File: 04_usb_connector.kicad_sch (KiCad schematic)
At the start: 2 parts

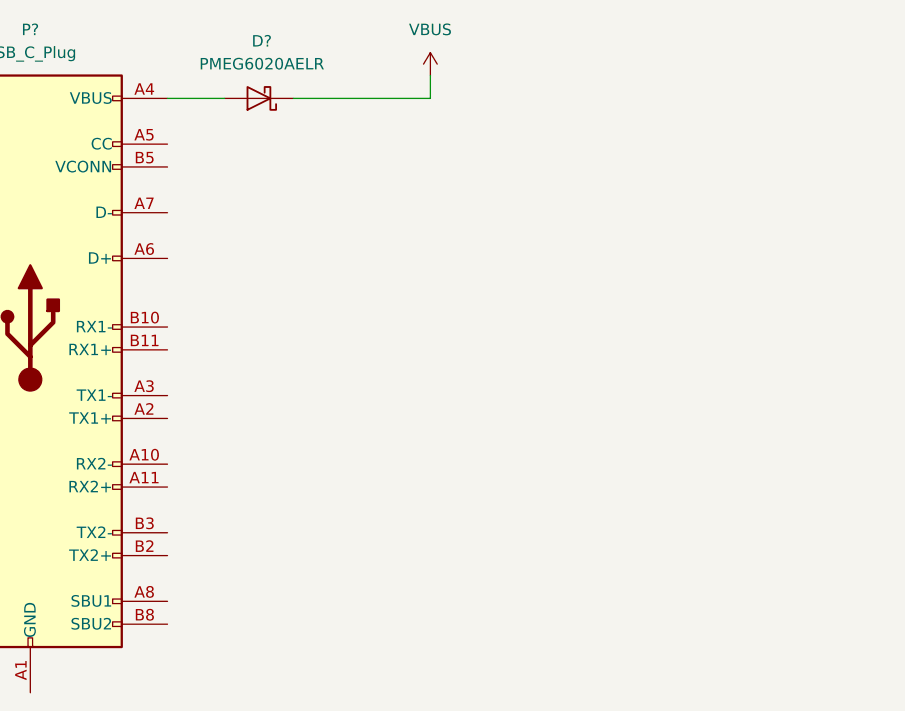
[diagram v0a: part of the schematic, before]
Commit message: added usb-c connector
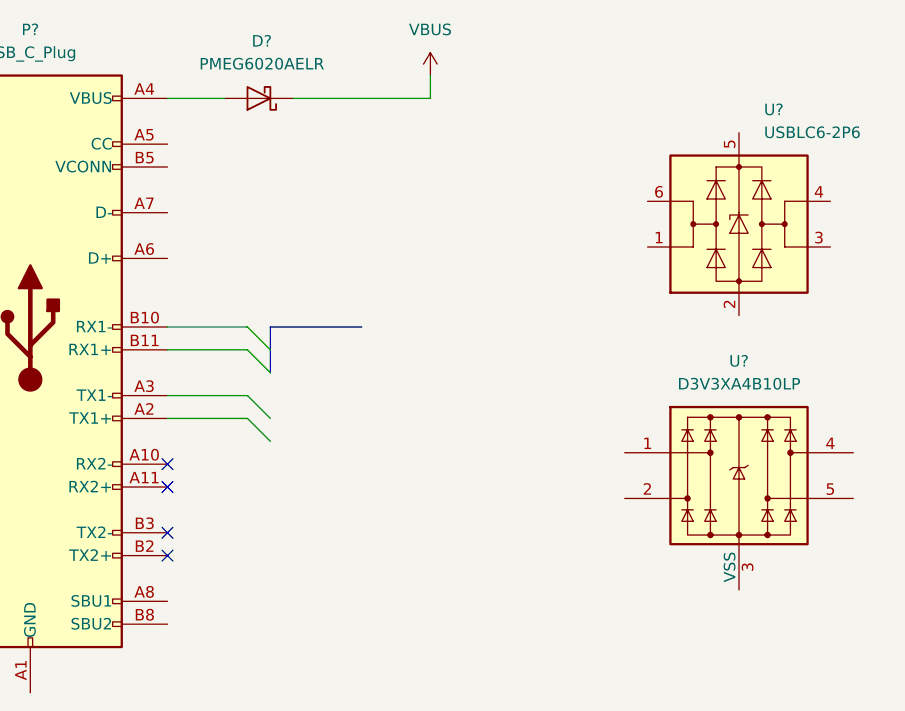
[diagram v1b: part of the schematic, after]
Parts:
- added U?: D3V3XA4B10LP, Package_DFN_QFN:Diodes_UDFN-10_1.0x2.5mm_P0.5mm, symbol Power_Protection:D3V3XA4B10LP
- added U?: USBLC6-2P6, Package_TO_SOT_SMD:SOT-666, symbol Power_Protection:USBLC6-2P6
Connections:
- new net: U?.3 (VSS), U?.8 (VSS)
- no-connect marks 0 -> 4
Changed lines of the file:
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@@
 (kicad_sch (version 20211123) (generator eeschema)
   (paper "A4")
+  (no_connect (at 86.36 96.52))
+  (no_connect (at 86.36 99.06))
+  (no_connect (at 86.36 106.68))
+  (no_connect (at 86.36 104.14))
+  (bus_entry (at 95.25 83.82) (size 2.54 2.54)
+    (stroke (width 0) (type default) (color 0 0 0 0))
+  )
+  (bus_entry (at 95.25 91.44) (size 2.54 2.54)
+    (stroke (width 0) (type default) (color 0 0 0 0))
+  )
+  (bus_entry (at 95.25 81.28) (size 2.54 2.54)
+    (stroke (width 0) (type default) (color 0 0 0 0))
+  )
+  (bus_entry (at 95.25 88.9) (size 2.54 2.54)
+    (stroke (width 0) (type default) (color 0 0 0 0))
+  )
+  (wire (pts (xy 86.36 91.44) (xy 95.25 91.44))
+    (stroke (width 0) (type default) (color 0 0 0 0))
+  )
   (wire (pts (xy 86.36 55.88) (xy 92.71 55.88))
+    (stroke (width 0) (type default) (color 0 0 0 0))
+  )
+  (bus (pts (xy 97.79 81.28) (xy 107.95 81.28))
+    (stroke (width 0) (type default) (color 0 0 0 0))
+  )
+  (wire (pts (xy 86.36 81.28) (xy 95.25 81.28))
     (stroke (width 0) (type default) (color 0 0 0 0))
   )
@@
     (stroke (width 0) (type default) (color 0 0 0 0))
   )
+  (wire (pts (xy 86.36 83.82) (xy 95.25 83.82))
+    (stroke (width 0) (type default) (color 0 0 0 0))
+  )
   (wire (pts (xy 100.33 55.88) (xy 115.57 55.88))
+    (stroke (width 0) (type default) (color 0 0 0 0))
+  )
+  (bus (pts (xy 97.79 86.36) (xy 97.79 83.82))
+    (stroke (width 0) (type default) (color 0 0 0 0))
+  )
+  (wire (pts (xy 86.36 88.9) (xy 95.25 88.9))
+    (stroke (width 0) (type default) (color 0 0 0 0))
+  )
+  (bus (pts (xy 97.79 83.82) (xy 97.79 81.28))
     (stroke (width 0) (type default) (color 0 0 0 0))
   )
@@
     )
     (pin "1")
+  )
+  (symbol (lib_id "Power_Protection:D3V3XA4B10LP") (at 149.86 97.79 0) (unit 1)
+    (in_bom yes) (on_board yes) (fields_autoplaced)
+    (property "Reference" "U?" (id 0) (at 149.86 85.09 0))
+    (property "Value" "D3V3XA4B10LP" (id 1) (at 149.86 87.63 0))
+    (property "Footprint" "Package_DFN_QFN:Diodes_UDFN-10_1.0x2.5mm_P0.5mm" (id 2) (at 125.73 107.95 0)
+      (effects (font (size 1.27 1.27)) hide)
+    )
+    (property "Datasheet" "https://www.diodes.com/assets/Datasheets/D3V3XA4B10LP.pdf" (id 3) (at 149.86 97.79 0)
+      (effects (font (size 1.27 1.27)) hide)
+    )
+    (pin "1")
+    (pin "10")
+    (pin "2")
+    (pin "3")
+    (pin "4")
+    (pin "5")
+    (pin "6")
+    (pin "7")
+    (pin "8")
+    (pin "9")
   )
   (symbol (lib_id "Connector:USB_C_Plug") (at 71.12 81.28 0) (unit 1)
@@
     (pin "S1")
   )
+  (symbol (lib_id "Power_Protection:USBLC6-2P6") (at 149.86 69.85 0) (unit 1)
+    (in_bom yes) (on_board yes) (fields_autoplaced)
+    (property "Reference" "U?" (id 0) (at 152.6287 57.15 0)
+      (effects (font (size 1.27 1.27)) (justify left))
+    )
+    (property "Value" "USBLC6-2P6" (id 1) (at 152.6287 59.69 0)
+      (effects (font (size 1.27 1.27)) (justify left))
+    )
+    (property "Footprint" "Package_TO_SOT_SMD:SOT-666" (id 2) (at 149.86 82.55 0)
+      (effects (font (size 1.27 1.27)) hide)
+    )
+    (property "Datasheet" "https://www.st.com/resource/en/datasheet/usblc6-2.pdf" (id 3) (at 154.94 60.96 0)
+      (effects (font (size 1.27 1.27)) hide)
+    )
+    (pin "1")
+    (pin "2")
+    (pin "3")
+    (pin "4")
+    (pin "5")
+    (pin "6")
+  )
   (symbol (lib_id "Diode:PMEG6020AELR") (at 96.52 55.88 180) (unit 1)

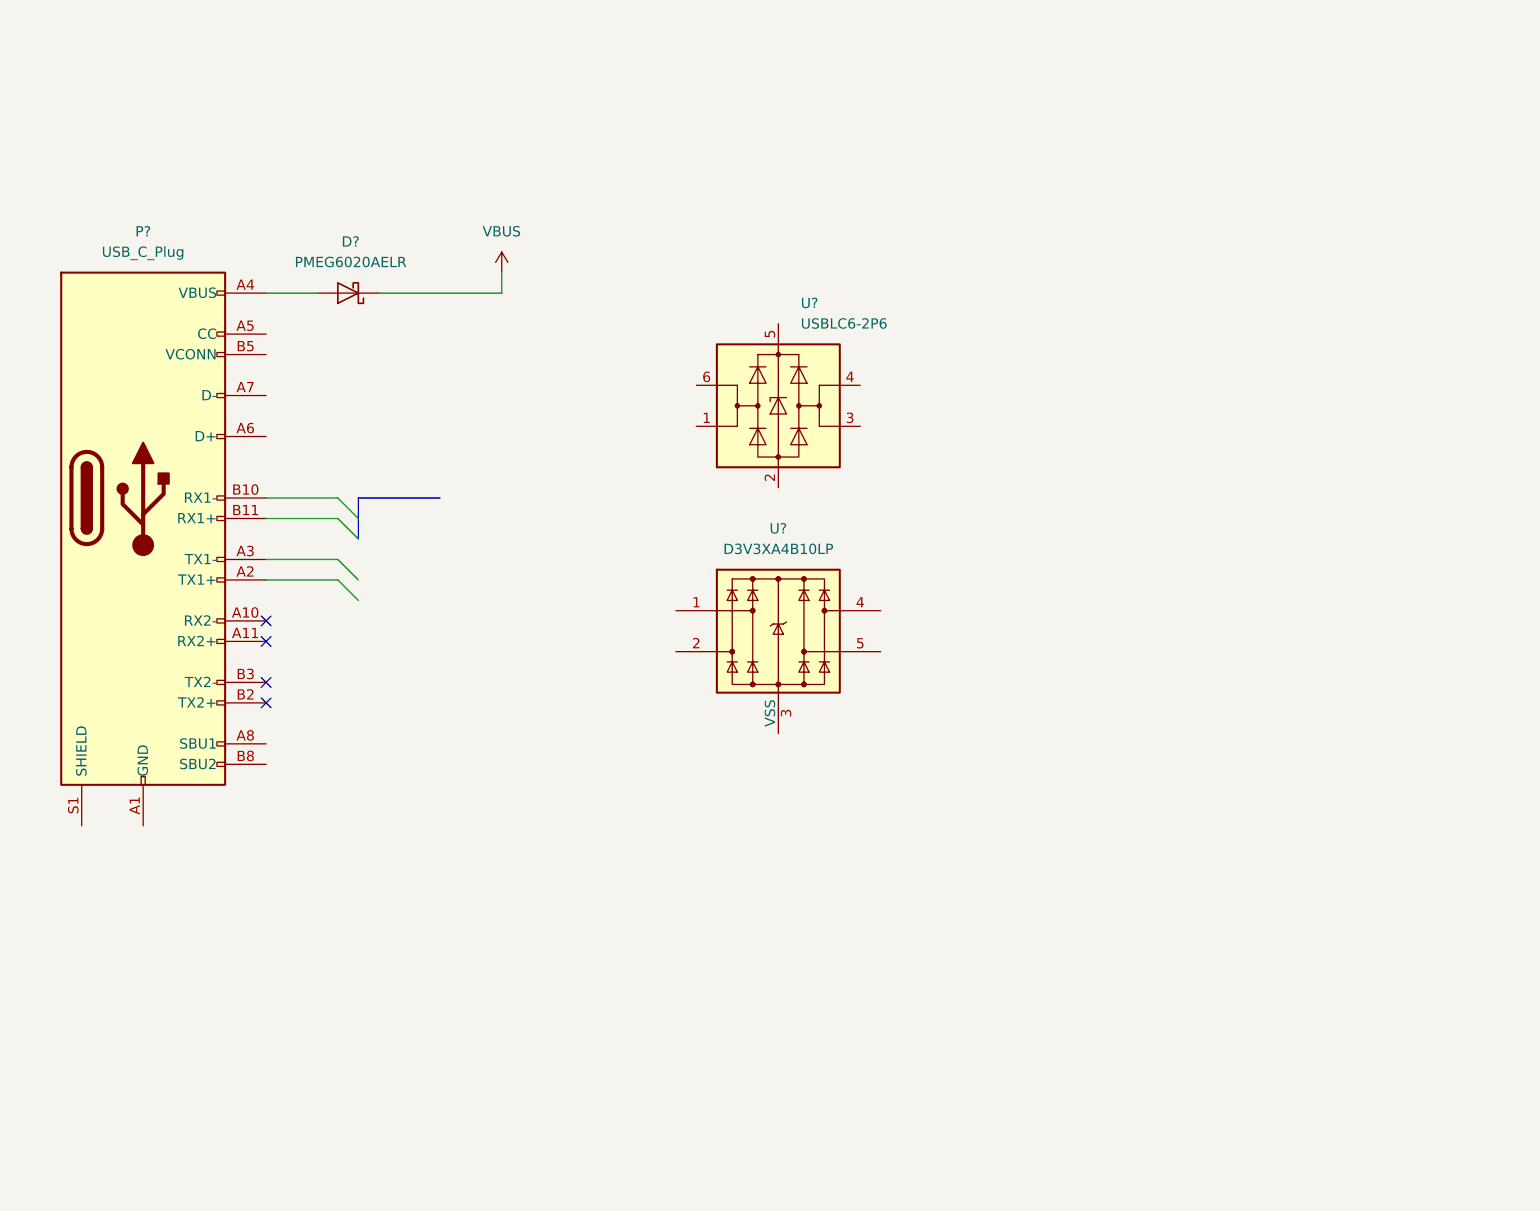
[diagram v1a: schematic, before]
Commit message: finished usb interface and added some new components
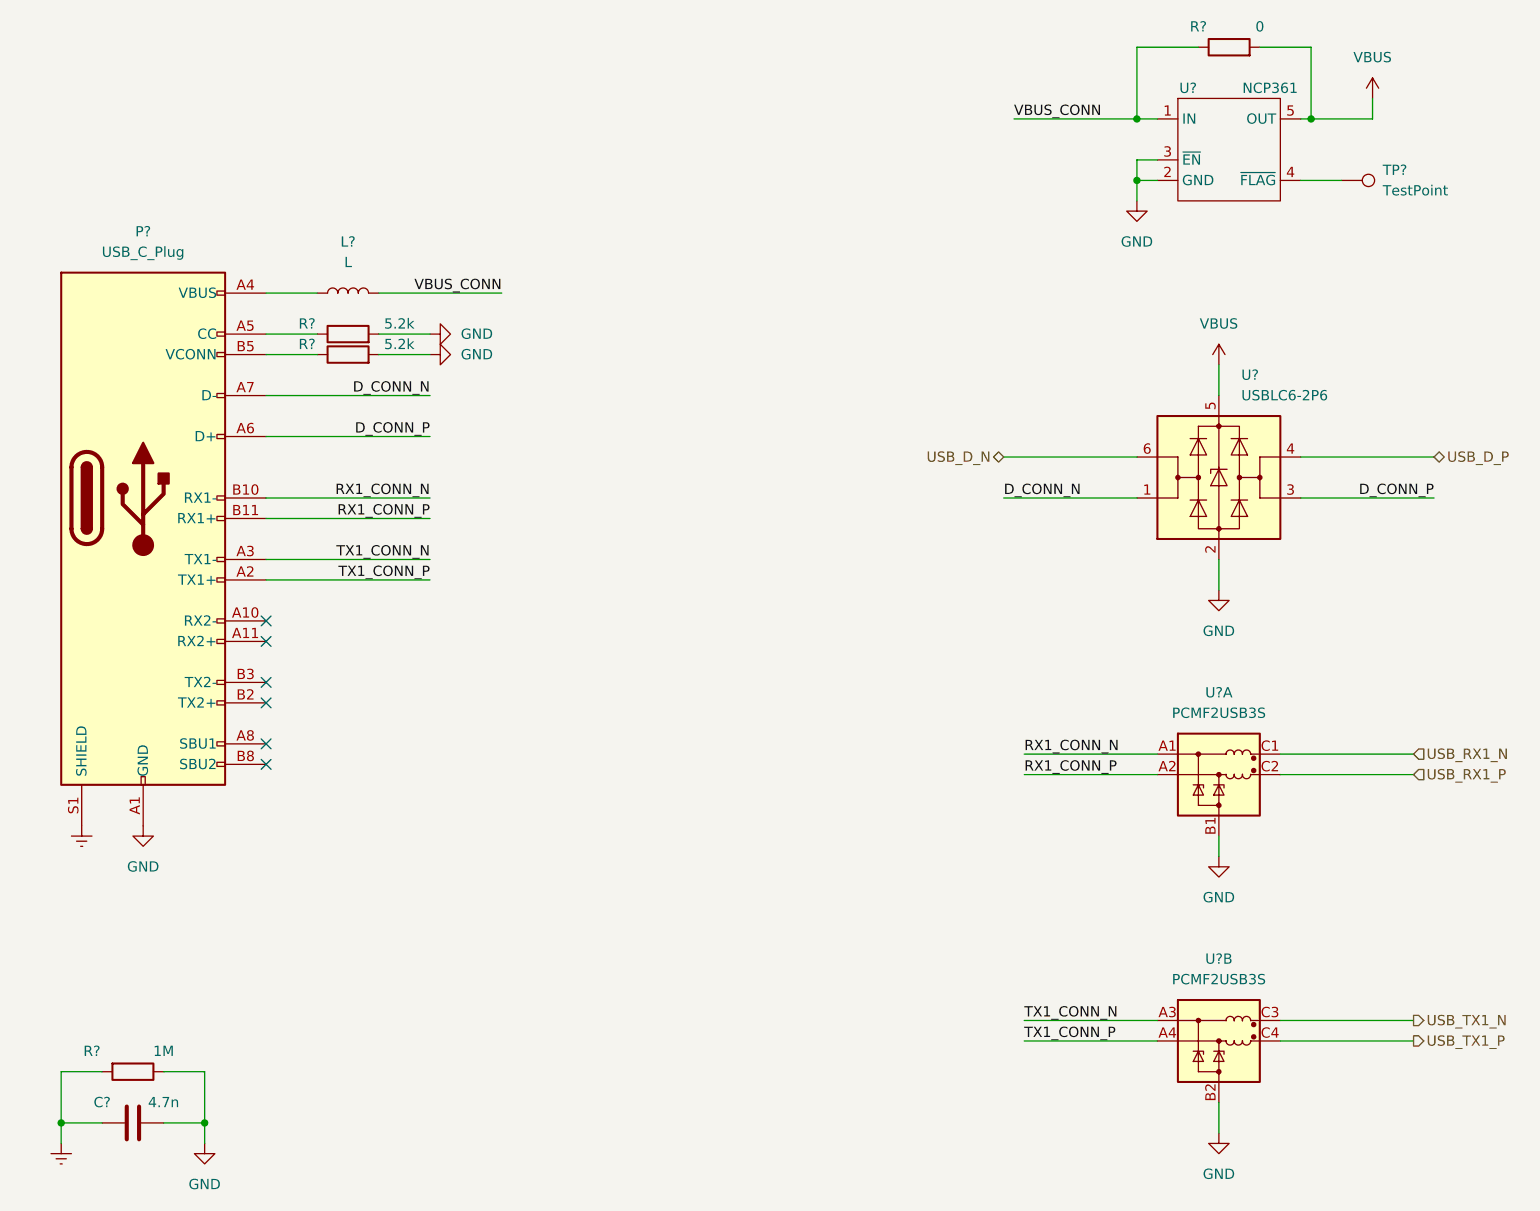
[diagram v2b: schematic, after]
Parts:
- removed D?: PMEG6020AELR, Diode_SMD:Nexperia_CFP3_SOD-123W, symbol Diode:PMEG6020AELR
- removed U?: D3V3XA4B10LP, Package_DFN_QFN:Diodes_UDFN-10_1.0x2.5mm_P0.5mm, symbol Power_Protection:D3V3XA4B10LP
- removed U?: USBLC6-2P6, Package_TO_SOT_SMD:SOT-666, symbol Power_Protection:USBLC6-2P6
- added C?: 4.7n, symbol Device:C
- added L?: L, Inductor_SMD:L_0603_1608Metric, symbol Device:L
- added R? (x2): 5.2k, Resistor_SMD:R_0603_1608Metric, symbol Device:R
- added R?: 1M, Resistor_SMD:R_0603_1608Metric, symbol Device:R
- added R?: 0, symbol Device:R
- added TP?: TestPoint, symbol Connector:TestPoint
- added U? (x2): PCMF2USB3S, samaritan:Nexperia_WLCSP-10_4-2-4_1.57x1.17mm_Layout6x3_P0.4mm, symbol samaritan:PCMF2USB3S
- added U?: USBLC6-2P6, Package_TO_SOT_SMD:SOT-666, symbol Power_Protection:USBLC6-2P6
- added U?: NCP361, samaritan:udfn-6_2x2, symbol samaritan:NCP361
- P?: footprint (none) -> Connector_USB:USB_C_Receptacle_GCT_USB4105-xx-A_16P_TopMnt_Horizontal
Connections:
- net VBUS: now also R?.2, U?.5 (OUT), U?.5 (VBUS)
- net GND: now reaches P?.A1 (GND), P?.A12 (GND), P?.B1 (GND), P?.B12 (GND)
- net GND: now also C?.2, R?.1, R?.2, R?.2, U?.2 (GND), U?.2 (GND), U?.3 (~{EN}), U?.B1 (GND_CH2), U?.B2 (GND_CH2)
- net TX1_CONN_P: now reaches P?.A2 (TX1+)
- net TX1_CONN_P: now also U?.A4 (CH2_IN-)
- net TX1_CONN_N: now reaches P?.A3 (TX1-)
- net TX1_CONN_N: now also U?.A3 (CH2_IN+)
- net at P?.A4 (VBUS), P?.A9 (VBUS), P?.B4 (VBUS)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: now also L?.1
- net at P?.A5 (CC): now also R?.1
- net D_CONN_P: now reaches P?.A6 (D+)
- net D_CONN_P: now also U?.3 (I/O2)
- net D_CONN_N: now reaches P?.A7 (D-)
- net D_CONN_N: now also U?.1 (I/O1)
- net RX1_CONN_N: now reaches P?.B10 (RX1-)
- net RX1_CONN_N: now also U?.A1 (CH2_IN+)
- net RX1_CONN_P: now reaches P?.B11 (RX1+)
- net RX1_CONN_P: now also U?.A2 (CH2_IN-)
- net at P?.B5 (VCONN): now also R?.1
- net Earth: now reaches P?.S1 (SHIELD)
- net Earth: now also C?.1, R?.2
- new net: TP?.1, U?.4 (~{FLAG})
- new net USB_D_N: U?.6 (I/O1)
- new net USB_D_P: U?.4 (I/O2)
- new net USB_RX1_N: U?.C1 (CH2_OUT+)
- new net USB_RX1_P: U?.C2 (CH2_OUT-)
- new net USB_TX1_N: U?.C3 (CH2_OUT+)
- new net USB_TX1_P: U?.C4 (CH2_OUT-)
- new net VBUS_CONN: L?.2, R?.1, U?.1 (IN)
- no-connect marks 4 -> 6

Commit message: finished first pass of the schematics
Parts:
- removed C?: 4.7n, symbol Device:C
- R?: value 1M -> 0
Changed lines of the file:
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@@
   (junction (at 194.31 34.29) (diameter 0) (color 0 0 0 0)
   )
-  (junction (at 60.96 158.75) (diameter 0) (color 0 0 0 0)
-  )
   (junction (at 215.9 34.29) (diameter 0) (color 0 0 0 0)
-  )
-  (junction (at 78.74 158.75) (diameter 0) (color 0 0 0 0)
   )
   (junction (at 194.31 41.91) (diameter 0) (color 0 0 0 0)
@@
     (stroke (width 0) (type default) (color 0 0 0 0))
   )
-  (wire (pts (xy 60.96 152.4) (xy 60.96 158.75))
-    (stroke (width 0) (type default) (color 0 0 0 0))
-  )
-  (wire (pts (xy 60.96 158.75) (xy 60.96 161.29))
-    (stroke (width 0) (type default) (color 0 0 0 0))
-  )
-  (wire (pts (xy 73.66 158.75) (xy 78.74 158.75))
+  (wire (pts (xy 60.96 152.4) (xy 60.96 161.29))
     (stroke (width 0) (type default) (color 0 0 0 0))
   )
@@
     (stroke (width 0) (type default) (color 0 0 0 0))
   )
-  (wire (pts (xy 78.74 158.75) (xy 78.74 161.29))
+  (wire (pts (xy 78.74 152.4) (xy 78.74 161.29))
     (stroke (width 0) (type default) (color 0 0 0 0))
   )
@@
     (stroke (width 0) (type default) (color 0 0 0 0))
   )
-  (wire (pts (xy 78.74 152.4) (xy 78.74 158.75))
-    (stroke (width 0) (type default) (color 0 0 0 0))
-  )
   (wire (pts (xy 212.09 115.57) (xy 228.6 115.57))
     (stroke (width 0) (type default) (color 0 0 0 0))
@@
   )
   (wire (pts (xy 212.09 113.03) (xy 228.6 113.03))
-    (stroke (width 0) (type default) (color 0 0 0 0))
-  )
-  (wire (pts (xy 60.96 158.75) (xy 66.04 158.75))
     (stroke (width 0) (type default) (color 0 0 0 0))
   )
@@
     (effects (font (size 1.27 1.27)) (justify left bottom))
   )
-  (hierarchical_label "USB_TX1_N" (shape output) (at 228.6 146.05 0)
+  (hierarchical_label "USB_TX1_N" (shape input) (at 228.6 146.05 0)
     (effects (font (size 1.27 1.27)) (justify left))
   )
-  (hierarchical_label "USB_RX1_N" (shape input) (at 228.6 113.03 0)
+  (hierarchical_label "USB_RX1_N" (shape output) (at 228.6 113.03 0)
     (effects (font (size 1.27 1.27)) (justify left))
   )
@@
     (effects (font (size 1.27 1.27)) (justify left))
   )
-  (hierarchical_label "USB_TX1_P" (shape output) (at 228.6 148.59 0)
+  (hierarchical_label "USB_TX1_P" (shape input) (at 228.6 148.59 0)
     (effects (font (size 1.27 1.27)) (justify left))
   )
-  (hierarchical_label "USB_RX1_P" (shape input) (at 228.6 115.57 0)
+  (hierarchical_label "USB_RX1_P" (shape output) (at 228.6 115.57 0)
     (effects (font (size 1.27 1.27)) (justify left))
   )
@@
     (in_bom yes) (on_board yes)
     (property "Reference" "R?" (id 0) (at 64.77 149.86 90))
-    (property "Value" "1M" (id 1) (at 73.66 149.86 90))
+    (property "Value" "0" (id 1) (at 73.66 149.86 90))
     (property "Footprint" "Resistor_SMD:R_0603_1608Metric" (id 2) (at 69.85 150.622 90)
       (effects (font (size 1.27 1.27)) hide)
@@
       (effects (font (size 1.27 1.27)) hide)
     )
-    (pin "1")
-    (pin "2")
-  )
-  (symbol (lib_id "Device:C") (at 69.85 158.75 90) (unit 1)
-    (in_bom yes) (on_board yes)
-    (property "Reference" "C?" (id 0) (at 66.04 156.21 90))
-    (property "Value" "4.7n" (id 1) (at 73.66 156.21 90))
-    (property "Footprint" "" (id 2) (at 73.66 157.7848 0)
-      (effects (font (size 1.27 1.27)) hide)
-    )
-    (property "Datasheet" "~" (id 3) (at 69.85 158.75 0)
-      (effects (font (size 1.27 1.27)) hide)
-    )
